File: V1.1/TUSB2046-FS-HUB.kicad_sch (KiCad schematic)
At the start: 66 parts, among them IC1 TUSB2046BVFR, J1 USB_B_Mini, J2 USB_A, J3 USB_A, J4 USB_A, J5 USB_A, J6 Conn_01x03, J7 Conn_01x03, J8 Conn_01x03, J9 Conn_01x03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

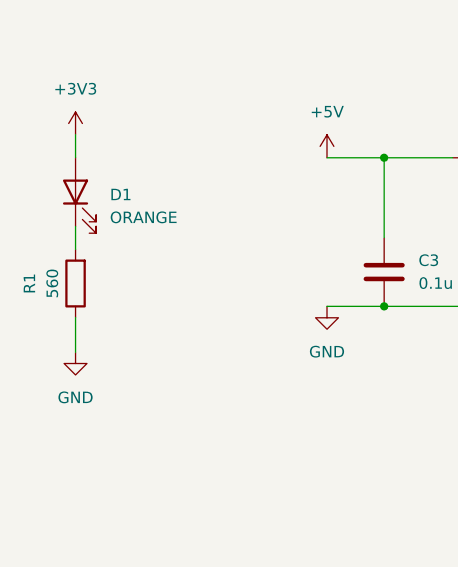
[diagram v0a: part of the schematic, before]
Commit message: Adjusted LED brightness
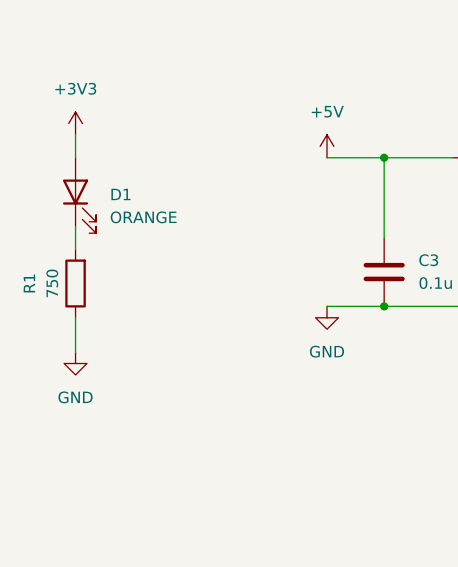
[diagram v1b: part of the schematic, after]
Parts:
- R1: value 560 -> 750
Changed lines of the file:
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@@
     (in_bom yes) (on_board yes)
     (property "Reference" "R1" (id 0) (at 20.32 50.8 90))
-    (property "Value" "560" (id 1) (at 22.86 50.8 90))
+    (property "Value" "750" (id 1) (at 22.86 50.8 90))
     (property "Footprint" "Resistor_SMD:R_0805_2012Metric" (id 2) (at 27.178 50.8 90)
       (effects (font (size 1.27 1.27)) hide)
@@
     )
     (path "/d2585116-e3d0-441e-ad43-ba85fd2a7165"
-      (reference "R1") (unit 1) (value "560") (footprint "Resistor_SMD:R_0805_2012Metric")
+      (reference "R1") (unit 1) (value "750") (footprint "Resistor_SMD:R_0805_2012Metric")
     )
     (path "/2d87ccc0-d321-4030-b172-e79164d6fb32"
